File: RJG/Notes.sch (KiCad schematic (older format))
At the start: 16 parts, among them SW301 Reload, U301 74HCT4051, U302 74HCT40105, U303 74LS157, U304 74LS157

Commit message: Small improvements
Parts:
- added C301, C302, C303, C304: 100n, Capacitor_THT:C_Disc_D7.0mm_W2.5mm_P5.00mm, symbol Device:C
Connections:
- net +5V: now also C301.2, C302.2, C303.2, C304.2
- net GND: now also C301.1, C302.1, C303.1, C304.1

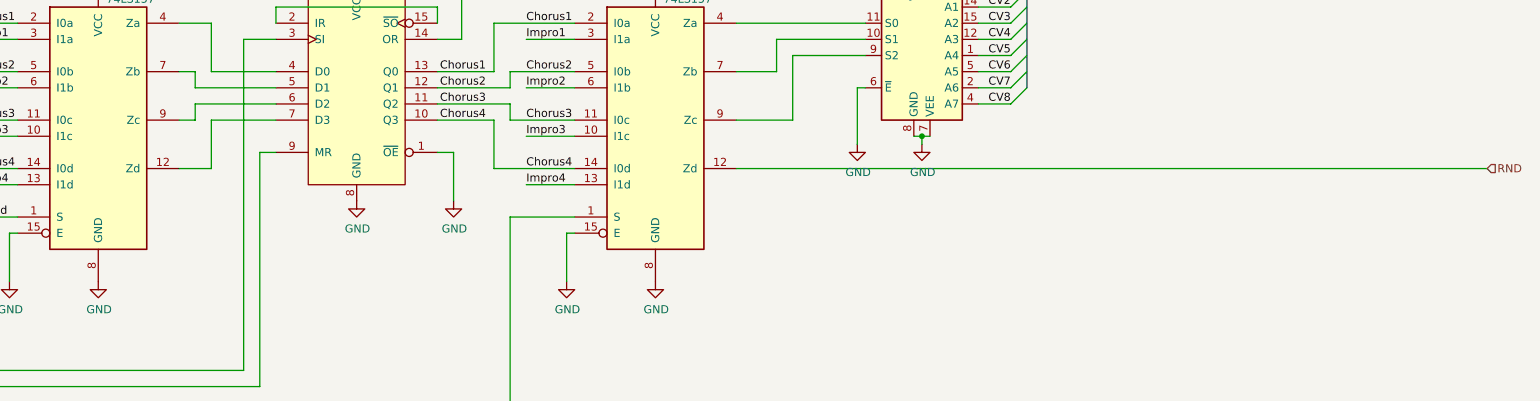
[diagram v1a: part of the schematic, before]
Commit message: Schematic done
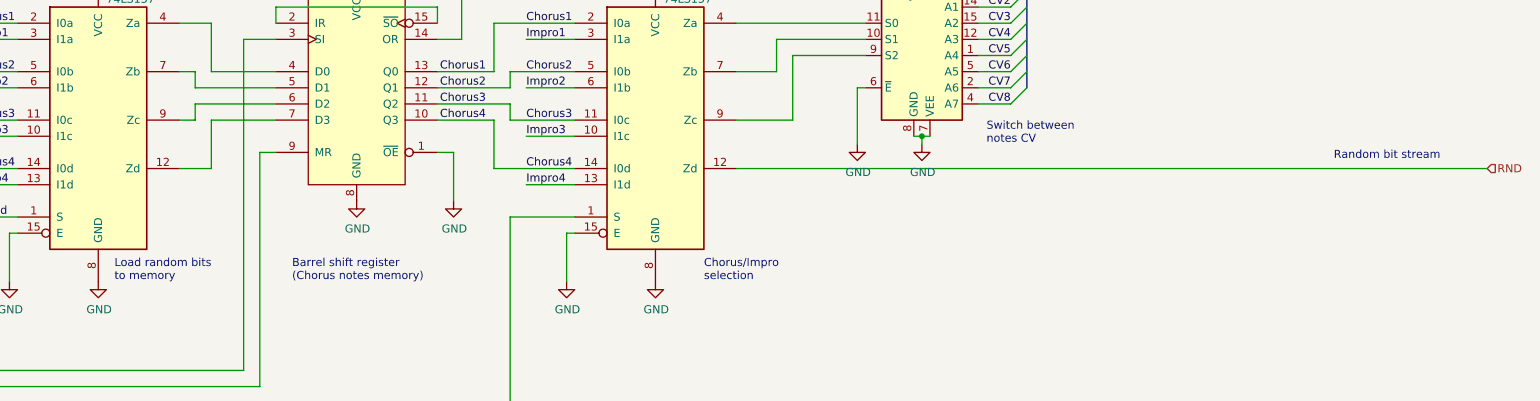
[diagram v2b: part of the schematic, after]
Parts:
- D301: footprint (none) -> LED_THT:LED_D3.0mm
- RV301, RV302, RV303, RV304, RV305, RV306, RV307, RV308: footprint Potentiometer_THT:Potentiometer_Alpha_RD901F-40-00D_Single_Vertical -> Potentiometer_THT:Potentiometer_Alps_RK09K_Single_Vertical
- SW301: footprint (none) -> Button_Switch_THT:SW_PUSH_6mm
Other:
- note added: "Barrel shift register\n(Chorus notes memory)"
- note added: "Chorus/Impro\nselection"
- note added: "Load random bits\nto memory"
- note added: "Random bit stream"
- note added: "Switch between\nnotes CV"
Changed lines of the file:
@@
 F 0 "D301" V 4539 1883 50  0000 R CNN
 F 1 "LED" V 4448 1883 50  0000 R CNN
-F 2 "" H 4500 2000 50  0001 C CNN
+F 2 "LED_THT:LED_D3.0mm" H 4500 2000 50  0001 C CNN
 F 3 "~" H 4500 2000 50  0001 C CNN
 	1    4500 2000
@@
 F 0 "SW301" H 2050 1385 50  0000 C CNN
 F 1 "Reload" H 2050 1294 50  0000 C CNN
-F 2 "" H 2050 1150 50  0001 C CNN
+F 2 "Button_Switch_THT:SW_PUSH_6mm" H 2050 1150 50  0001 C CNN
 F 3 "~" H 2050 1150 50  0001 C CNN
 	1    2050 1150
@@
 F 0 "RV308" H 9931 1096 50  0000 R CNN
 F 1 "100k" H 9931 1005 50  0000 R CNN
-F 2 "Potentiometer_THT:Potentiometer_Alpha_RD901F-40-00D_Single_Vertical" H 10000 1050 50  0001 C CNN
+F 2 "Potentiometer_THT:Potentiometer_Alps_RK09K_Single_Vertical" H 10000 1050 50  0001 C CNN
 F 3 "~" H 10000 1050 50  0001 C CNN
 	1    10000 1050
@@
 F 0 "RV307" H 9231 1096 50  0000 R CNN
 F 1 "100k" H 9231 1005 50  0000 R CNN
-F 2 "Potentiometer_THT:Potentiometer_Alpha_RD901F-40-00D_Single_Vertical" H 9300 1050 50  0001 C CNN
+F 2 "Potentiometer_THT:Potentiometer_Alps_RK09K_Single_Vertical" H 9300 1050 50  0001 C CNN
 F 3 "~" H 9300 1050 50  0001 C CNN
 	1    9300 1050
@@
 F 0 "RV306" H 8531 1096 50  0000 R CNN
 F 1 "100k" H 8531 1005 50  0000 R CNN
-F 2 "Potentiometer_THT:Potentiometer_Alpha_RD901F-40-00D_Single_Vertical" H 8600 1050 50  0001 C CNN
+F 2 "Potentiometer_THT:Potentiometer_Alps_RK09K_Single_Vertical" H 8600 1050 50  0001 C CNN
 F 3 "~" H 8600 1050 50  0001 C CNN
 	1    8600 1050
@@
 F 0 "RV305" H 7831 1096 50  0000 R CNN
 F 1 "100k" H 7831 1005 50  0000 R CNN
-F 2 "Potentiometer_THT:Potentiometer_Alpha_RD901F-40-00D_Single_Vertical" H 7900 1050 50  0001 C CNN
+F 2 "Potentiometer_THT:Potentiometer_Alps_RK09K_Single_Vertical" H 7900 1050 50  0001 C CNN
 F 3 "~" H 7900 1050 50  0001 C CNN
 	1    7900 1050
@@
 F 0 "RV304" H 7131 1096 50  0000 R CNN
 F 1 "100k" H 7131 1005 50  0000 R CNN
-F 2 "Potentiometer_THT:Potentiometer_Alpha_RD901F-40-00D_Single_Vertical" H 7200 1050 50  0001 C CNN
+F 2 "Potentiometer_THT:Potentiometer_Alps_RK09K_Single_Vertical" H 7200 1050 50  0001 C CNN
 F 3 "~" H 7200 1050 50  0001 C CNN
 	1    7200 1050
@@
 F 0 "RV303" H 6431 1096 50  0000 R CNN
 F 1 "100k" H 6431 1005 50  0000 R CNN
-F 2 "Potentiometer_THT:Potentiometer_Alpha_RD901F-40-00D_Single_Vertical" H 6500 1050 50  0001 C CNN
+F 2 "Potentiometer_THT:Potentiometer_Alps_RK09K_Single_Vertical" H 6500 1050 50  0001 C CNN
 F 3 "~" H 6500 1050 50  0001 C CNN
 	1    6500 1050
@@
 F 0 "RV302" H 5731 1096 50  0000 R CNN
 F 1 "100k" H 5731 1005 50  0000 R CNN
-F 2 "Potentiometer_THT:Potentiometer_Alpha_RD901F-40-00D_Single_Vertical" H 5800 1050 50  0001 C CNN
+F 2 "Potentiometer_THT:Potentiometer_Alps_RK09K_Single_Vertical" H 5800 1050 50  0001 C CNN
 F 3 "~" H 5800 1050 50  0001 C CNN
 	1    5800 1050
@@
 F 0 "RV301" H 5031 1096 50  0000 R CNN
 F 1 "100k" H 5031 1005 50  0000 R CNN
-F 2 "Potentiometer_THT:Potentiometer_Alpha_RD901F-40-00D_Single_Vertical" H 5100 1050 50  0001 C CNN
+F 2 "Potentiometer_THT:Potentiometer_Alps_RK09K_Single_Vertical" H 5100 1050 50  0001 C CNN
 F 3 "~" H 5100 1050 50  0001 C CNN
 	1    5100 1050
@@
 Wire Bus Line
 	8000 1450 8000 2900
+Text Notes 2350 4100 0    50   ~ 0
+Load random bits\nto memory
+Text Notes 3450 4100 0    50   ~ 0
+Barrel shift register\n(Chorus notes memory)
+Text Notes 6000 4100 0    50   ~ 0
+Chorus/Impro\nselection
+Text Notes 7750 3250 0    50   ~ 0
+Switch between\nnotes CV
+Text Notes 9900 3350 0    50   ~ 0
+Random bit stream
 $EndSCHEMATC

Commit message: Layout improvment
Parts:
- D301: footprint LED_THT:LED_D3.0mm -> LED_SMD:LED_1206_3216Metric_ReverseMount_Hole1.8x2.4mm
- R302: footprint Resistor_THT:R_Axial_DIN0204_L3.6mm_D1.6mm_P7.62mm_Horizontal -> Resistor_SMD:R_1206_3216Metric_Pad1.42x1.75mm_HandSolder
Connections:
- net Chorus2: now also U303.14 (I0d), U304.14 (I0d); no longer U303.5 (I0b), U304.5 (I0b)
- net Chorus3: now also U303.5 (I0b), U304.5 (I0b); no longer U303.11 (I0c), U304.11 (I0c)
- net Chorus4: now also U303.11 (I0c), U304.11 (I0c); no longer U303.14 (I0d), U304.14 (I0d)
- net Rb2: now also U303.13 (I1d), U304.13 (I1d); no longer U303.6 (I1b), U304.6 (I1b)
- net Rb3: now also U303.6 (I1b), U304.6 (I1b); no longer U303.10 (I1c), U304.10 (I1c)
- net Rb4: now also U303.10 (I1c), U304.10 (I1c); no longer U303.13 (I1d), U304.13 (I1d)
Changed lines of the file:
@@
 F 0 "R302" H 4570 1696 50  0000 L CNN
 F 1 "1k" H 4570 1605 50  0000 L CNN
-F 2 "Resistor_THT:R_Axial_DIN0204_L3.6mm_D1.6mm_P7.62mm_Horizontal" V 4430 1650 50  0001 C CNN
+F 2 "Resistor_SMD:R_1206_3216Metric_Pad1.42x1.75mm_HandSolder" V 4430 1650 50  0001 C CNN
 F 3 "~" H 4500 1650 50  0001 C CNN
 	1    4500 1650
@@
 U 1 1 5F5E61CF
 P 4500 2000
-F 0 "D301" V 4539 1883 50  0000 R CNN
-F 1 "LED" V 4448 1883 50  0000 R CNN
-F 2 "LED_THT:LED_D3.0mm" H 4500 2000 50  0001 C CNN
+F 0 "D301" V 4539 1882 50  0000 R CNN
+F 1 "LED" V 4448 1882 50  0000 R CNN
+F 2 "LED_SMD:LED_1206_3216Metric_ReverseMount_Hole1.8x2.4mm" H 4500 2000 50  0001 C CNN
 F 3 "~" H 4500 2000 50  0001 C CNN
 	1    4500 2000
@@
 $EndComp
 Wire Wire Line
-	4700 3400 5200 3400
-Wire Wire Line
-	4350 3100 4700 3100
-Wire Wire Line
-	4700 3100 4700 3400
-Wire Wire Line
-	4800 3100 5200 3100
-Wire Wire Line
-	4350 3000 4800 3000
-Wire Wire Line
-	4800 3000 4800 3100
-Wire Wire Line
-	4800 2800 5200 2800
-Wire Wire Line
-	4350 2900 4800 2900
-Wire Wire Line
-	4800 2900 4800 2800
-Wire Wire Line
-	4700 2500 5200 2500
-Wire Wire Line
-	4350 2800 4700 2800
-Wire Wire Line
-	4700 2800 4700 2500
+	4900 3400 5200 3400
+Wire Wire Line
+	4350 3100 4650 3100
+Wire Wire Line
+	4900 2800 5200 2800
+Wire Wire Line
+	4350 3000 4650 3000
+Wire Wire Line
+	4900 3100 5200 3100
+Wire Wire Line
+	4350 2900 4650 2900
+Wire Wire Line
+	4900 2500 5200 2500
+Wire Wire Line
+	4350 2800 4650 2800
 Wire Wire Line
 	3250 3300 3250 4750
@@
 Impro1
 Wire Wire Line
+	5200 3200 4900 3200
+Text Label 4900 3400 0    50   ~ 0
+Chorus2
+Text Label 4900 3500 0    50   ~ 0
+Impro2
+Wire Wire Line
 	5200 2900 4900 2900
 Text Label 4900 2800 0    50   ~ 0
-Chorus2
+Chorus3
 Text Label 4900 2900 0    50   ~ 0
-Impro2
-Wire Wire Line
-	5200 3200 4900 3200
+Impro3
+Wire Wire Line
+	5200 3500 4900 3500
 Text Label 4900 3100 0    50   ~ 0
-Chorus3
+Chorus4
 Text Label 4900 3200 0    50   ~ 0
-Impro3
-Wire Wire Line
-	5200 3500 4900 3500
-Text Label 4900 3400 0    50   ~ 0
-Chorus4
-Text Label 4900 3500 0    50   ~ 0
 Impro4
 Text Label 4650 2800 2    50   ~ 0
@@
 Wire Wire Line
 	1750 3700 1450 3700
-Text Label 1450 3500 0    50   ~ 0
+Text Label 1450 3200 0    50   ~ 0
 Impro4
-Text Label 1450 3400 0    50   ~ 0
+Text Label 1450 3100 0    50   ~ 0
 Chorus4
-Wire Wire Line
-	1750 3500 1450 3500
-Wire Wire Line
-	1750 3400 1450 3400
-Text Label 1450 3200 0    50   ~ 0
-Impro3
-Text Label 1450 3100 0    50   ~ 0
-Chorus3
 Wire Wire Line
 	1750 3200 1450 3200
@@
 	1750 3100 1450 3100
 Text Label 1450 2900 0    50   ~ 0
+Impro3
+Text Label 1450 2800 0    50   ~ 0
+Chorus3
+Wire Wire Line
+	1750 2900 1450 2900
+Wire Wire Line
+	1750 2800 1450 2800
+Text Label 1450 3500 0    50   ~ 0
 Impro2
-Text Label 1450 2800 0    50   ~ 0
+Text Label 1450 3400 0    50   ~ 0
 Chorus2
 Wire Wire Line
-	1750 2900 1450 2900
-Wire Wire Line
-	1750 2800 1450 2800
+	1750 3500 1450 3500
+Wire Wire Line
+	1750 3400 1450 3400
 Text Label 1450 2600 0    50   ~ 0
 Impro1
@@
 	1    0    0    -1
 $EndComp
-Wire Bus Line
-	5550 1450 8000 1450
-Wire Bus Line
-	8000 1450 10250 1450
-Wire Bus Line
-	8000 1450 8000 2900
 Text Notes 2350 4100 0    50   ~ 0
 Load random bits\nto memory
@@
 Text Notes 9900 3350 0    50   ~ 0
 Random bit stream
+Wire Bus Line
+	5550 1450 8000 1450
+Wire Bus Line
+	8000 1450 10250 1450
+Wire Bus Line
+	8000 1450 8000 2900
 $EndSCHEMATC

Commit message: Finsihed layout
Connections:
- net at U301.11 (S0): now also U304.9 (Zc); no longer U304.4 (Za)
- net at U301.9 (S2): now also U304.4 (Za); no longer U304.9 (Zc)
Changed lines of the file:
@@
 	6450 2600 7000 2600
 Wire Wire Line
-	6200 3100 6550 3100
-Wire Wire Line
-	6550 3100 6550 2700
-Wire Wire Line
-	6550 2700 7000 2700
-Wire Wire Line
-	6200 2500 7000 2500
+	6200 3100 6650 3100
 Wire Wire Line
 	7700 2300 7900 2300
@@
 Text Notes 9900 3350 0    50   ~ 0
 Random bit stream
+Wire Wire Line
+	6650 2500 7000 2500
+Wire Wire Line
+	6650 2500 6650 3100
+Wire Wire Line
+	7000 2700 6550 2700
+Wire Wire Line
+	6550 2700 6550 2500
+Wire Wire Line
+	6550 2500 6200 2500
 Wire Bus Line
 	5550 1450 8000 1450

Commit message: Corrected error
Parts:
- added D302, D303, D304, D305: LED, LED_SMD:LED_1206_3216Metric_ReverseMount_Hole1.8x2.4mm, symbol Device:LED
- added R303, R304, R305, R306: 1k, Resistor_SMD:R_1206_3216Metric_Pad1.42x1.75mm_HandSolder, symbol Device:R
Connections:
- net Chorus2: now also U303.5 (I0b); no longer U303.14 (I0d)
- net Chorus3: now also U303.11 (I0c); no longer U303.5 (I0b)
- net Chorus4: now also U303.14 (I0d); no longer U303.11 (I0c)
- net GND: now also D302.1 (K), D303.1 (K), D304.1 (K), D305.1 (K)
- net RND: now also R306.1
- net S1: now reaches U301.10 (S1), U304.7 (Zb)
- net S1: now also R304.1
- net S0: now reaches U301.11 (S0), U304.9 (Zc)
- net S0: now also R303.1
- net S2: now reaches U301.9 (S2), U304.4 (Za)
- net S2: now also R305.1
- net Full: now reaches D301.1 (K), U302.14 (OR)
- new net: D302.2 (A), R303.2
- new net: D303.2 (A), R304.2
- new net: D304.2 (A), R305.2
- new net: D305.2 (A), R306.2
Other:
- moved on the sheet: D301, R302, U304

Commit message: Minor tweaks; added BOM
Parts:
- U303, U304: value 74LS157 -> 74HCT157
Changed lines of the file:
@@
 AR Path="/5F424A92/5F4279E7" Ref="U304"  Part="1"
 F 0 "U304" H 6000 3950 50  0000 C CNN
-F 1 "74LS157" H 6050 3850 50  0000 C CNN
+F 1 "74HCT157" H 6050 3850 50  0000 C CNN
 F 2 "Package_DIP:DIP-16_W7.62mm_LongPads" H 5850 3100 50  0001 C CNN
 F 3 "http://www.ti.com/lit/gpn/sn74LS157" H 5850 3100 50  0001 C CNN
@@
 AR Path="/5F424A92/5F4F7408" Ref="U303"  Part="1"
 F 0 "U303" H 2400 3950 50  0000 C CNN
-F 1 "74LS157" H 2450 3850 50  0000 C CNN
+F 1 "74HCT157" H 2450 3850 50  0000 C CNN
 F 2 "Package_DIP:DIP-16_W7.62mm_LongPads" H 2250 3100 50  0001 C CNN
 F 3 "http://www.ti.com/lit/gpn/sn74LS157" H 2250 3100 50  0001 C CNN

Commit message: fix stuffs
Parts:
- added C?: 1u, Capacitor_THT:CP_Radial_D8.0mm_P3.80mm, symbol Device:CP
- added C?: 10u, Capacitor_THT:CP_Radial_D8.0mm_P3.80mm, symbol Device:CP
- added D? (x2): 1N4148, Diode_THT:D_DO-35_SOD27_P7.62mm_Horizontal, symbol Diode:1N4148
- added R?: 100k, Resistor_THT:R_Axial_DIN0204_L3.6mm_D1.6mm_P7.62mm_Horizontal, symbol Device:R
- added R? (x2): 47k, Resistor_THT:R_Axial_DIN0204_L3.6mm_D1.6mm_P7.62mm_Horizontal, symbol Device:R
- added U?: 74HCT194, symbol 74xx:74LS194
- added U? (x2): NE555, symbol Timer:NE555
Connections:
- net +5V: now also R301.1, R?.1, R?.1, U?.1 (Mr), U?.10 (S1), U?.16 (VCC), U?.2 (Dsr), U?.4 (R), U?.4 (R), U?.7 (Dsl), U?.8 (VCC), U?.8 (VCC), U?.9 (S0); no longer SW301.1 (A)
- net Clk: now also U?.2 (TR); no longer U302.3 (SI)
- net Full: now also U302.2 (IR); no longer U302.14 (OR)
- net GND: now also SW301.1 (A), C?.2, C?.2, R?.2, U?.1 (GND), U?.1 (GND), U?.8 (GND); no longer R301.2
- net Reload: now also D?.2 (A), U?.3 (Q); no longer R301.1, SW301.2 (B)
- net at U303.12 (Zd): now also U?.6 (P3); no longer U302.7 (D3)
- net at U303.4 (Za): now also U?.3 (P0); no longer U302.4 (D0)
- net at U303.7 (Zb): now also U?.4 (P1); no longer U302.5 (D1)
- net at U303.9 (Zc): now also U?.5 (P2); no longer U302.6 (D2)
- net ~Barrel~\Shift: now reaches U302.15 (~SO)
- net ~Barrel~\Shift: now also D?.1 (K), D?.1 (K), R?.1; no longer U302.2 (IR)
- new net: R301.2, SW301.2 (B), U?.2 (TR)
- new net: U302.4 (D0), U?.15 (Q0)
- new net: U302.5 (D1), U?.14 (Q1)
- new net: U302.6 (D2), U?.13 (Q2)
- new net: U302.7 (D3), U?.12 (Q3)
- new net: C?.1, R?.2, U?.6 (THR), U?.7 (DIS) (x2)
- new net Clk_Clean: D?.2 (A), U302.3 (SI), U?.3 (Q)
- new net PreClk: U?.11 (Cp)
- no-connect marks 0 -> 3
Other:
- note added: "0 1 2 0 1 2 3"
- note added: "17bits total, but as the input is\nthe same as the output, only\n16bits effective"
- note added: "4*1bit register"
- note added: "Apparently the FIFO needs that,\nmaybe for buffering, maybe\nbecause it invert the signal..."
- note added: "Barrel shift register (4*16bits)\n(Chorus notes memory)"
- note added: "Clk"
- note added: "Clk_Clean"
- note added: "Main Clock"
- note added: "Monostable \nfor debouncing"
- note added: "PreClk"
- note added: "Pressing the reload button will prevent\nthe clock (by holding it high) to go \nto the Shift Output,\nallowing the register to fill up"
- note removed: "Barrel shift register\n(Chorus notes memory)"
- moved on the sheet: C301, C302, C303, C304, D301, D302, D303, D304, D305, R301, R302, R303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
